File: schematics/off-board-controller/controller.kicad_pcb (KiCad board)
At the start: 2 copper layers, 90 x 60 mm, 61 parts, among them J1 programmer, J2 5-1814832-1, J3 xt60, SW5 SW_SPDT_MSM, U4 STM32L476RGTx, U5 RFM98W-433S2, U6 L78L33_TO92, U8 MCP23S17_SP, U9 MCP23S17_SP

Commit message: layout
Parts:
- removed R28: 470, Resistor_SMD:R_0805_2012Metric_Pad1.20x1.40mm_HandSolder
- added R2: 470, Resistor_SMD:R_0805_2012Metric_Pad1.20x1.40mm_HandSolder, F.Cu at (71.8, 169.1)
- moved R37 214.5 mm to (57.8, 172.1)
- moved R38 211.3 mm to (57.8, 169.1)
- moved R39 208.2 mm to (57.8, 166.1)
- moved R40 205.3 mm to (57.8, 163.1)
- moved R41 202.9 mm to (57.8, 161.1)
- moved R35 201.7 mm to (57.8, 176.1)
- moved R36 199.3 mm to (57.8, 174.1), turned to 180 degrees
- moved R31 195.2 mm to (71.8, 174.1), turned to 180 degrees
- moved R30 195.1 mm to (71.8, 171.1)
- moved R33 194.7 mm to (71.8, 179.1), turned to 180 degrees
- moved R32 194.6 mm to (71.8, 176.1)
- moved R34 194.1 mm to (71.8, 181.1), turned to 180 degrees
- moved R27 194.0 mm to (71.8, 163.1)
- moved R19 187.1 mm to (58.8, 138.1), turned to 180 degrees
- moved R20 184.6 mm to (58.8, 135.1), turned to 180 degrees
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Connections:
- R1 pad 1: Net-(R1-Pad1) -> Net-(U10-3f)
- U9 pad 25: Net-(U10-3e) -> Net-(U9-GPA4)
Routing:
- net Net-(U5-ANT): track 0.00 -> 6.80 mm

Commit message: made plan for layout
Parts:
- moved J3 225.0 mm to (23.5, 88.5)
- moved U6 216.8 mm to (26.7, 78.9)
- moved U4 203.3 mm to (56.5, 96.0)
- moved C12 187.4 mm to (40.5, 40.0), turned to -90 degrees
- moved J1 165.6 mm to (88.5, 106.5), turned to -90 degrees
- moved S3 153.3 mm to (110.5, 56.5)
- moved S2 151.6 mm to (110.5, 86.5)
- moved S1 150.0 mm to (111.0, 72.0)
- moved C14 143.6 mm to (87.5, 41.5), turned to 180 degrees
- moved R33 141.7 mm to (26.7, 44.7), turned to 0 degrees
- moved R34 139.9 mm to (40.5, 44.7)
- moved R32 136.6 mm to (26.7, 47.1)
- moved R31 132.3 mm to (26.7, 49.7), turned to 0 degrees
- moved R35 130.1 mm to (40.5, 47.1), turned to 180 degrees
- moved R30 127.2 mm to (26.7, 52.1)
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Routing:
- net Net-(U10-3e): track 0.00 -> 102.6 mm
- net Net-(U10-3d): track 0.00 -> 89.6 mm
- net Net-(U10-3c): track 0.00 -> 79.2 mm
- net Net-(U10-3b): track 0.00 -> 76.8 mm
- net Net-(U10-dp1): track 0.00 -> 64.8 mm
- net Net-(U10-3a): track 0.00 -> 61.8 mm
- net Net-(U10-2b): track 0.00 -> 58.2 mm, vias 0 -> 1
- net Net-(U10-2f): track 0.00 -> 56.1 mm, vias 0 -> 1
- net Net-(U10-2a): track 0.00 -> 53.1 mm, vias 0 -> 1
- net Net-(U10-dp3): track 0.00 -> 50.2 mm, vias 0 -> 1
- net Net-(U10-1b): track 0.00 -> 46.0 mm
- net Net-(U10-2e): track 0.00 -> 45.3 mm, vias 0 -> 1
- net Net-(U10-1g): track 0.00 -> 44.4 mm
- net Net-(U10-2g): track 0.00 -> 41.5 mm, vias 0 -> 1
- net Net-(U10-2d): track 0.00 -> 41.4 mm, vias 0 -> 1
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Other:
- board size 90 x 60 mm -> 110 x 90 mm

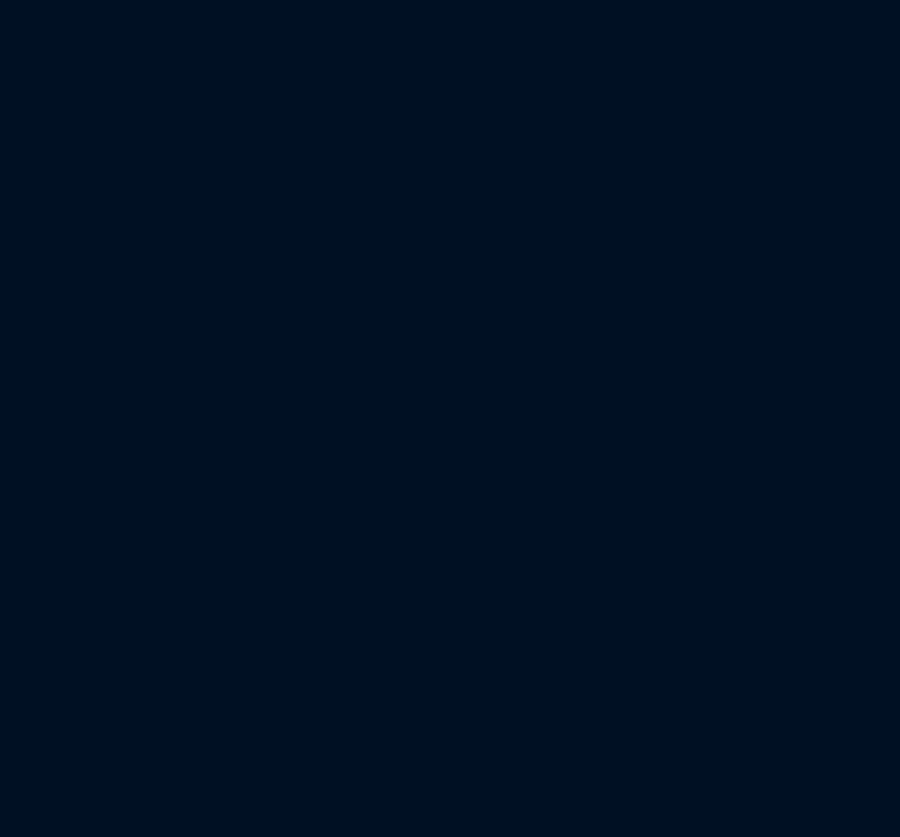
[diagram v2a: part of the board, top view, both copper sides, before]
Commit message: added some leds to controller
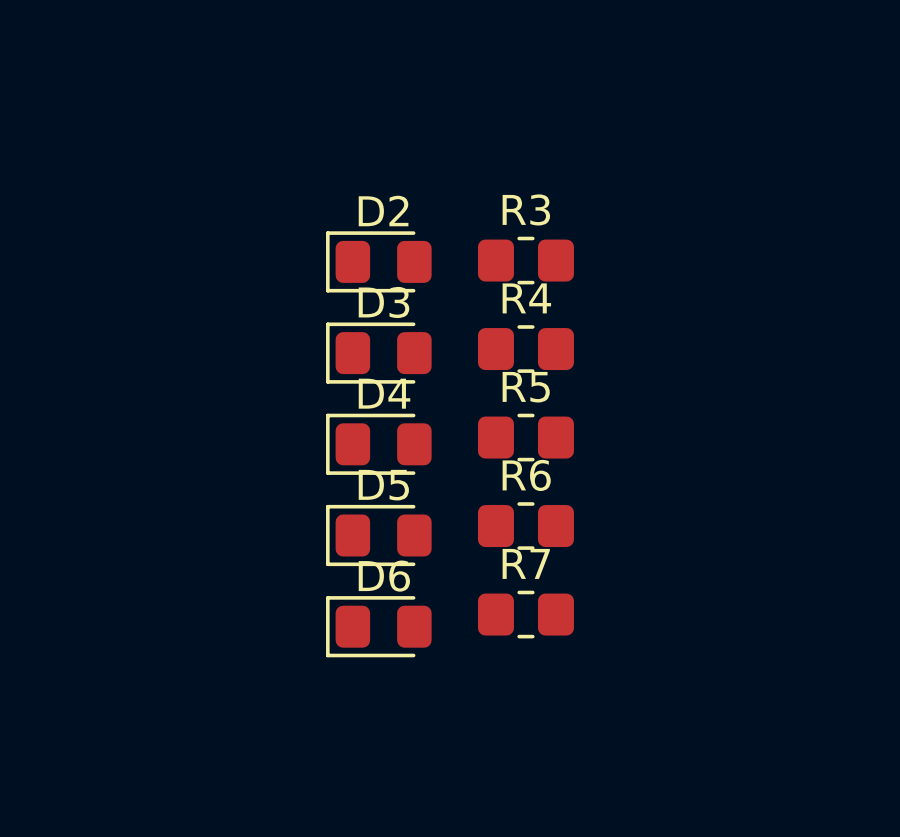
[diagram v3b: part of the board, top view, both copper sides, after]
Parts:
- added D2: LED, LED_SMD:LED_0805_2012Metric_Pad1.15x1.40mm_HandSolder, F.Cu at (216.8, 35.7)
- added D3: LED, LED_SMD:LED_0805_2012Metric_Pad1.15x1.40mm_HandSolder, F.Cu at (216.8, 38.8)
- added D4: LED, LED_SMD:LED_0805_2012Metric_Pad1.15x1.40mm_HandSolder, F.Cu at (216.8, 41.8)
- added D5: LED, LED_SMD:LED_0805_2012Metric_Pad1.15x1.40mm_HandSolder, F.Cu at (216.8, 44.9)
- added D6: LED, LED_SMD:LED_0805_2012Metric_Pad1.15x1.40mm_HandSolder, F.Cu at (216.8, 47.9)
- added R3: 330, Resistor_SMD:R_0805_2012Metric_Pad1.20x1.40mm_HandSolder, F.Cu at (221.5, 35.7)
- added R4: 330, Resistor_SMD:R_0805_2012Metric_Pad1.20x1.40mm_HandSolder, F.Cu at (221.5, 38.6)
- added R5: 330, Resistor_SMD:R_0805_2012Metric_Pad1.20x1.40mm_HandSolder, F.Cu at (221.5, 41.6)
- added R6: 330, Resistor_SMD:R_0805_2012Metric_Pad1.20x1.40mm_HandSolder, F.Cu at (221.5, 44.5)
- added R7: 330, Resistor_SMD:R_0805_2012Metric_Pad1.20x1.40mm_HandSolder, F.Cu at (221.5, 47.5)

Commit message: produced first draft of layout design
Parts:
- removed C11, C13: 100n, Capacitor_SMD:C_0805_2012Metric_Pad1.18x1.45mm_HandSolder
- added U1: ~, Connector:NS-Tech_Grove_1x04_P2mm_Vertical, F.Cu at (103.5, 106.5)
- J3: value xt60 -> 9V
- moved C2 220.8 mm to (23.5, 75.5), turned to 180 degrees
- moved D1 218.8 mm to (25.5, 83.5), turned to -90 degrees
- moved C3 215.7 mm to (29.0, 75.5), turned to 180 degrees
- moved R5 184.5 mm to (49.0, 107.0), turned to 180 degrees
- moved D4 176.3 mm to (53.0, 107.0)
- moved R3 174.0 mm to (63.0, 107.5), turned to 180 degrees
- moved D2 166.1 mm to (67.0, 107.5)
- moved R4 160.8 mm to (76.0, 107.0), turned to 180 degrees
- moved D3 152.8 mm to (80.0, 107.0)
- moved R9 145.4 mm to (108.5, 62.5), turned to 90 degrees
- moved C10 144.7 mm to (109.5, 33.5), turned to -90 degrees
- moved R6 144.6 mm to (89.0, 102.5), turned to -90 degrees
- moved C9 142.4 mm to (102.0, 68.5)
- moved D5 141.8 mm to (89.0, 106.5), turned to -90 degrees
- moved C7 141.8 mm to (102.0, 73.0)
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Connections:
- net Net-(D1-A) renamed /power/batt
- U4 pad 28: unconnected-(U4-PB2-Pad28) -> +3V3
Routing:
- net +3V3: track 20.2 -> 332.5 mm
- net MOSI: track 0.00 -> 160.6 mm
- net MISO: track 0.00 -> 159.9 mm
- net SCK: track 0.00 -> 131.6 mm
- net BTN_SEND_CODE: track 0.00 -> 15.6 mm
- net BTN_RELEASE_POD: track 0.00 -> 14.9 mm
- net BTN_REQ_CODE: track 0.00 -> 12.0 mm
- net +9V: track 0.00 -> 8.15 mm
- net TRISTATE_UP: track 0.00 -> 5.54 mm
- net TRISTATE_DOWN: track 0.00 -> 3.75 mm
- net /power/batt: track 0.00 -> 3.22 mm
- net /mcu/RESET: track 0.00 -> 3.16 mm
- net Net-(U4-BOOT0): track 0.00 -> 2.64 mm
- net Net-(D6-K): track 0.00 -> 1.95 mm
- net Net-(D5-K): track 0.00 -> 1.95 mm
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
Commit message: redesigned layout
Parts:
- moved J3 151.3 mm to (165.7, 132.9), turned to -90 degrees
- moved D1 147.2 mm to (165.2, 129.9), turned to 0 degrees
- moved C2 145.1 mm to (157.2, 131.9), turned to -90 degrees
- moved U6 139.7 mm to (160.2, 126.4), turned to -90 degrees
- moved C3 138.0 mm to (157.2, 126.5), turned to -90 degrees
- moved R26 116.4 mm to (130.7, 114.5), turned to 90 degrees
- moved R27 115.4 mm to (128.3, 114.5), turned to 90 degrees
- moved R1 114.4 mm to (125.8, 114.5), turned to 90 degrees
- moved R2 113.6 mm to (123.3, 114.5), turned to 90 degrees
- moved R30 112.8 mm to (120.7, 114.5), turned to 90 degrees
- moved R31 112.2 mm to (118.3, 114.5), turned to 90 degrees
- moved R32 111.6 mm to (115.7, 114.5), turned to 90 degrees
- moved R33 111.2 mm to (113.3, 114.5), turned to 90 degrees
- moved U9 102.0 mm to (130.6, 103.7), turned to -90 degrees
- moved R41 98.4 mm to (131.3, 100.7), turned to -90 degrees
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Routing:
- net RESET_IO: track 0.00 -> 121.7 mm, vias 0 -> 2
- net CS_RADIO: track 0.00 -> 69.9 mm, vias 0 -> 1
- net +3V3: track 332.5 -> 387.2 mm
- net RADIO_DONE: track 0.00 -> 53.5 mm, vias 0 -> 2
- net SCK: track 131.6 -> 170.9 mm, vias 0 -> 1
- net MOSI: track 160.6 -> 185.5 mm, vias 0 -> 1
- net MISO: track 159.9 -> 180.9 mm, vias 0 -> 1
- net /mcu/SWDIO: track 0.00 -> 18.1 mm, vias 0 -> 1
- net /mcu/SWCLK: track 0.00 -> 13.1 mm, vias 0 -> 1
- net Net-(U10-3f): track 33.2 -> 25.8 mm
- net Net-(U10-2c): track 30.9 -> 24.7 mm
- net BTN_REQ_CODE: track 12.0 -> 17.0 mm
- net Net-(U10-2g): track 41.5 -> 37.4 mm
- net Net-(U10-3g): track 36.8 -> 33.3 mm
- net Net-(U10-2f): track 56.1 -> 52.8 mm
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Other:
- board size 110 x 90 mm -> 80 x 90 mm

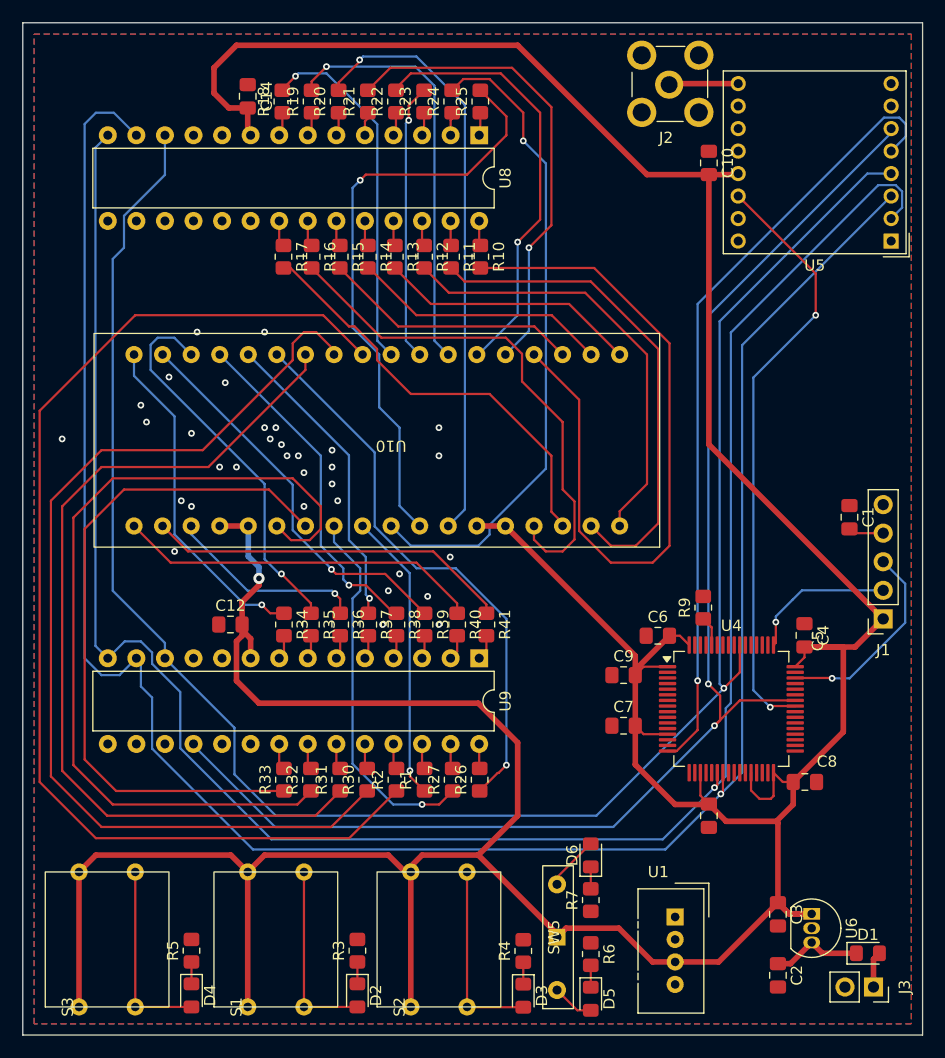
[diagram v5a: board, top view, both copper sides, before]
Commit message: first draft of off- board layout
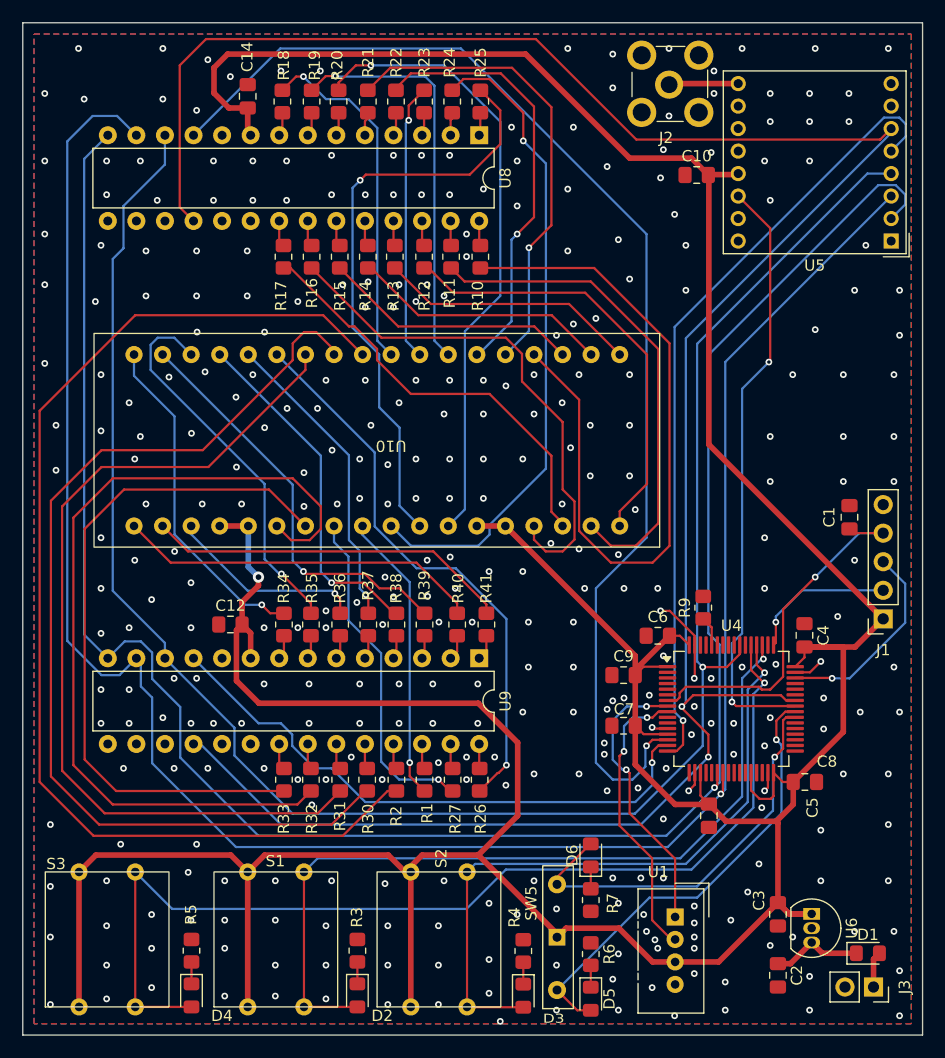
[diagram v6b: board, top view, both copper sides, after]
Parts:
- moved C10 1.52 mm to (150.0, 60.8), turned to 0 degrees
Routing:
- net CS_IO1-2: track 0.00 -> 108.6 mm, vias 0 -> 1
- net RESET_IO: track 121.7 -> 209.1 mm
- net BTN_RELEASE_POD: track 17.0 -> 92.5 mm, vias 0 -> 1
- net BTN_SEND_CODE: track 16.8 -> 72.9 mm, vias 0 -> 1
- net CS_IO3-4: track 0.00 -> 51.9 mm, vias 0 -> 1
- net BTN_REQ_CODE: track 17.0 -> 59.4 mm, vias 0 -> 1
- net TRISTATE_UP: track 3.75 -> 40.6 mm, vias 0 -> 1
- net TRISTATE_DOWN: track 4.86 -> 36.5 mm, vias 0 -> 1
- net /mcu/RESET: track 3.16 -> 32.4 mm, vias 0 -> 1
- net ADC_IN2: track 0.00 -> 25.8 mm, vias 0 -> 2
- net ADC_IN1: track 0.00 -> 25.4 mm, vias 0 -> 2
- net GND: track 0.00 -> 15.4 mm, vias 33 -> 354
- net Net-(U10-3g): track 33.3 -> 30.1 mm
- net Net-(U10-2f): track 52.8 -> 55.6 mm
- net MISO: track 180.9 -> 183.0 mm
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
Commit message: submitted version for checking
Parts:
- D1: footprint LED_SMD:LED_0805_2012Metric_Pad1.15x1.40mm_HandSolder -> Diode_THT:D_A-405_P7.62mm_Horizontal
- moved D1 3.73 mm to (167.0, 126.7), turned to -90 degrees
- moved J3 2.89 mm to (163.0, 134.0)
- moved S2 0.53 mm to (124.5, 135.2)
- moved S1 0.28 mm to (110.0, 135.0)
- moved S3 0.28 mm to (95.0, 135.0)
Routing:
- net +9V: track 8.15 -> 11.5 mm
- net +3V3: track 387.0 -> 388.2 mm
- net /power/batt: track 3.22 -> 4.12 mm
- net BTN_REQ_CODE: track 59.4 -> 60.1 mm
- net BTN_RELEASE_POD: track 92.5 -> 93.1 mm
